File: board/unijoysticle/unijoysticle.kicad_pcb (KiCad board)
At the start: 2 copper layers, 55.6 x 41.7 mm, 14 parts, among them IC1 7405, IC2 7405, J1 DB9_Female, J2 DB9_Female, J3 Barrel_Jack, SW1 SW_Push

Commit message: board: rev B ready ??
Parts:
- moved J3 0.85 mm to (161.2, 113.9)
- moved D3 0.38 mm to (160.5, 103.9)
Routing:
- net J2UP: track 14.1 -> 11.1 mm
- net GPIO_J2DOWN: track 12.4 -> 10.5 mm
- net GPIO_J2UP: track 13.1 -> 15.0 mm
- net J2RIGHT: track 27.4 -> 25.7 mm
- net GPIO_J1POTY: track 26.1 -> 27.6 mm
- net GPIO_J2FIRE: track 20.7 -> 22.2 mm
- net VDD: track 76.6 -> 77.9 mm
- net J1POTY: track 45.6 -> 45.1 mm

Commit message: layout: Rev C: Work in progress
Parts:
- removed G***: LOGO, Parts:unijoysticle_logo
- removed REF**: OSHW-Logo2_7.3x6mm_SilkScreen, Symbol:OSHW-Logo2_7.3x6mm_SilkScreen
- added D4: 1N4001, Diode_THT:D_DO-41_SOD81_P7.62mm_Horizontal, F.Cu at (153.7, 83.8)
- added SW2: SW_SPST, Button_Switch_THT:SW_DIP_SPSTx01_Slide_6.7x4.1mm_W7.62mm_P2.54mm_LowProfile, F.Cu at (133.3, 83.8)
- R1, R2: value 100 -> 150
- moved J3 3.24 mm to (162.6, 116.8)
- moved SW1 3.13 mm to (115.0, 116.5)
- moved R2 2.95 mm to (124.5, 118.0)
- moved R1 2.88 mm to (121.9, 118.0)
- moved B1 2.54 mm to (127.3, 125.7)
- moved D3 1.70 mm to (161.3, 105.4)
- moved IC1 1.52 mm to (115.6, 83.4)
- moved D1 1.45 mm to (116.8, 105.4)
- moved D2 1.26 mm to (123.2, 105.4)
- moved IC2 0.76 mm to (161.3, 83.4)
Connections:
- IC1 pad 14: VDD -> J1POWER
- IC2 pad 14: VDD -> Net-(IC2-Pad14)
- J1 pad 7: Net-(J1-Pad7) -> J1POWER
- J2 pad 7: Net-(J2-Pad7) -> J1POWER
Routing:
- net VDD: track 77.9 -> 0.00 mm
- net J1POTY: track 45.1 -> 0.00 mm
- net GPIO_J1POTY: track 27.6 -> 0.00 mm
- net J1FIRE: track 26.1 -> 0.00 mm
- net J2RIGHT: track 25.7 -> 0.00 mm
- net J2FIRE: track 25.5 -> 0.00 mm
- net GPIO_J1POTX: track 25.1 -> 0.00 mm
- net J1RIGHT: track 24.2 -> 0.00 mm
- net GPIO_J2FIRE: track 22.2 -> 0.00 mm
- net J1LEFT: track 21.8 -> 0.00 mm
- net GPIO_J1UP: track 20.9 -> 0.00 mm
- net J2LEFT: track 20.0 -> 0.00 mm
- net GPIO_J1FIRE: track 19.7 -> 0.00 mm
- net GPIO_J1DOWN: track 18.9 -> 0.00 mm
- net J1DOWN: track 17.5 -> 0.00 mm
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- removed copper zone on B.Cu, net GND
- removed copper zone on F.Cu, net GND
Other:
- board size 55.6 x 41.7 mm -> 58 x 44.4 mm
- board text added: "Rev C"
- board text removed: "Rev B"

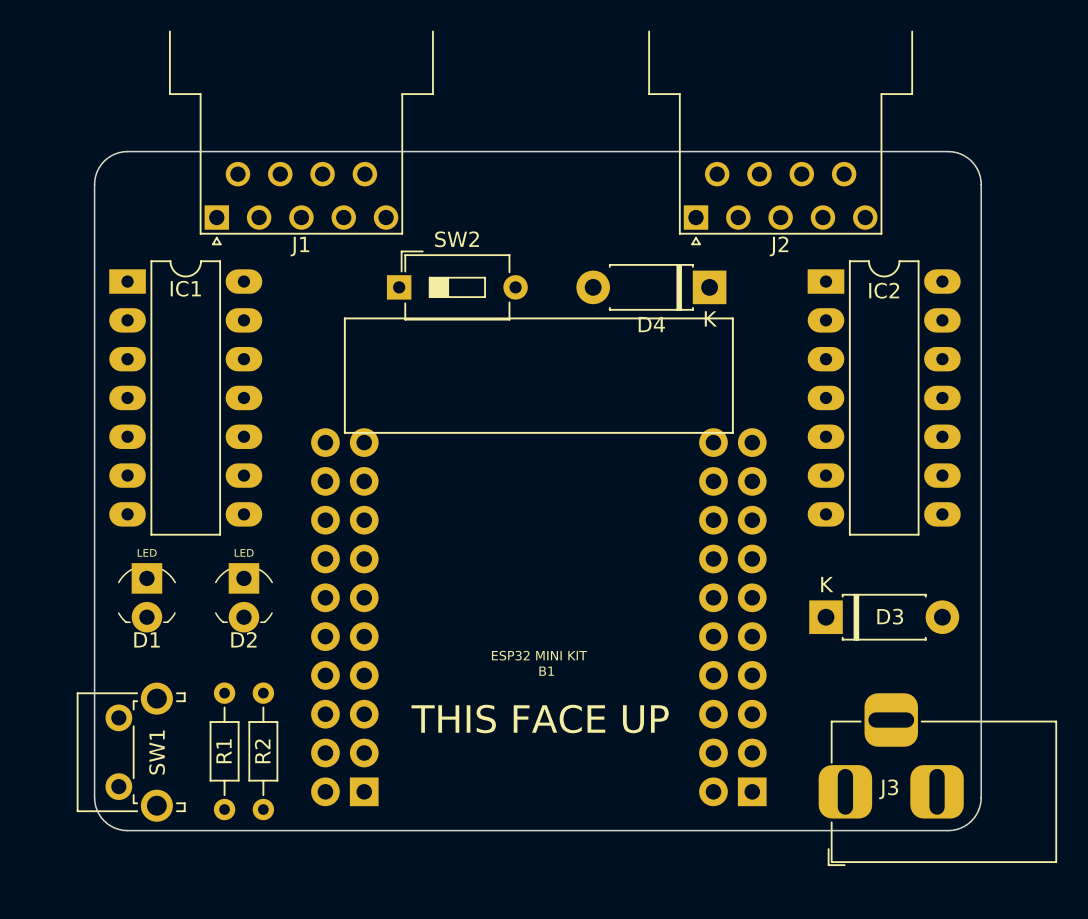
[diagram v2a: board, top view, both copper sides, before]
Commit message: layout / schematic: replaced 7405 model with one with comes with pwr/gnd
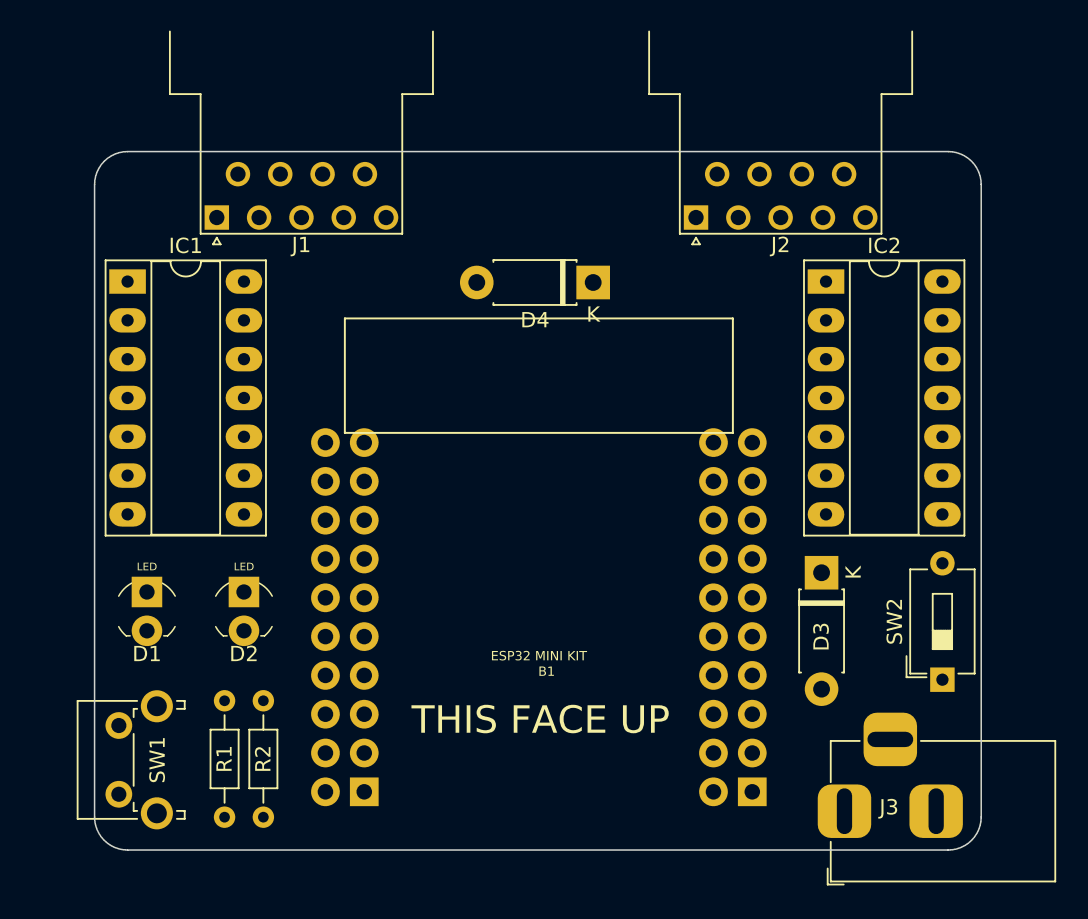
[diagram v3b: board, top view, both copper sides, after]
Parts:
- IC1, IC2: value 7405 -> 74LS05; footprint Package_DIP:DIP-14_W7.62mm_LongPads -> Package_DIP:DIP-14_W7.62mm_Socket_LongPads
- moved SW2 43.9 mm to (168.9, 109.5), turned to 90 degrees
- moved D4 7.63 mm to (146.1, 83.5)
- moved D3 2.92 mm to (161.0, 102.5), turned to 270 degrees
- moved J3 1.27 mm to (162.5, 118.1)
- moved D1 0.89 mm to (116.8, 106.3)
- moved D2 0.89 mm to (123.2, 106.3)
- moved R1 0.50 mm to (121.9, 118.5)
- moved R2 0.50 mm to (124.5, 118.5)
- moved SW1 0.50 mm to (115.0, 117.0)
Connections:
- B1 pad 11: Net-(B1-Pad11) -> (no net)
- B1 pad 15: Net-(B1-Pad15) -> (no net)
- B1 pad 21: Net-(B1-Pad21) -> (no net)
- B1 pad 22: Net-(B1-Pad22) -> (no net)
- B1 pad 3: Net-(B1-Pad3) -> (no net)
- B1 pad 34: Net-(B1-Pad34) -> (no net)
- B1 pad 35: Net-(B1-Pad35) -> (no net)
- B1 pad 36: Net-(B1-Pad36) -> (no net)
- B1 pad 39: Net-(B1-Pad39) -> (no net)
- B1 pad 4: Net-(B1-Pad4) -> (no net)
- B1 pad 6: Net-(B1-Pad6) -> (no net)
- B1 pad 7: Net-(B1-Pad7) -> (no net)
- B1 pad 8: Net-(B1-Pad8) -> (no net)
- B1 pad 9: Net-(B1-Pad9) -> (no net)
- D4 pad 1: VDD -> Net-(D4-Pad1)
- D4 pad 2: Net-(D4-Pad2) -> J1POWER
- IC2 pad 14: Net-(IC2-Pad14) -> J1POWER
- J2 pad 5: Net-(J2-Pad5) -> (no net)
- J2 pad 9: Net-(J2-Pad9) -> (no net)
- SW2 pad 1: J1POWER -> VDD
- SW2 pad 2: Net-(D4-Pad2) -> Net-(D4-Pad1)
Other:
- board size 58 x 44.4 mm -> 58 x 45.7 mm

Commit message: board: import unijoysticle logo
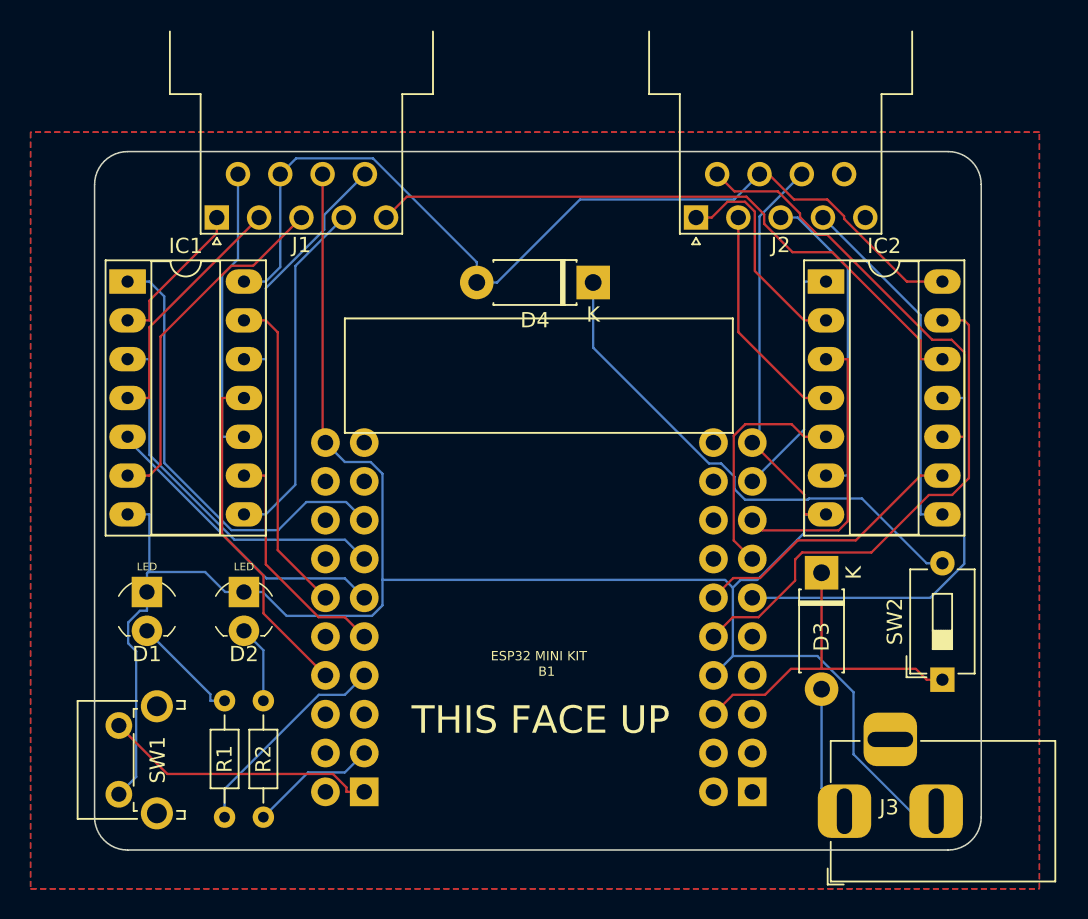
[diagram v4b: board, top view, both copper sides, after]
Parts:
- added G***: LOGO, Unijoysticle:unijoysticle_logo, B.Cu at (142.2, 96.5)
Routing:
- net GND: track 0.00 -> 153.5 mm
- net J1POWER: track 0.00 -> 62.7 mm
- net J1POTY: track 0.00 -> 42.5 mm
- net GPIO_J1POTY: track 0.00 -> 33.7 mm
- net Net-(D4-Pad1): track 0.00 -> 33.5 mm
- net GPIO_J1UP: track 0.00 -> 29.9 mm
- net J2FIRE: track 0.00 -> 28.1 mm
- net GPIO_J2FIRE: track 0.00 -> 27.1 mm
- net GPIO_J1DOWN: track 0.00 -> 24.6 mm
- net J2RIGHT: track 0.00 -> 23.5 mm
- net J1LEFT: track 0.00 -> 23.3 mm
- net J1RIGHT: track 0.00 -> 23.0 mm
- net VDD: track 0.00 -> 22.8 mm
- net GPIO_J1FIRE: track 0.00 -> 22.4 mm
- net GPIO_J1POTX: track 0.00 -> 21.2 mm
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- added copper zone on B.Cu, net GND
- added copper zone on F.Cu, net GND

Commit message: board: rev D
changes DIP switch for slide switch since it supports more amperage
board a tiny bit wider
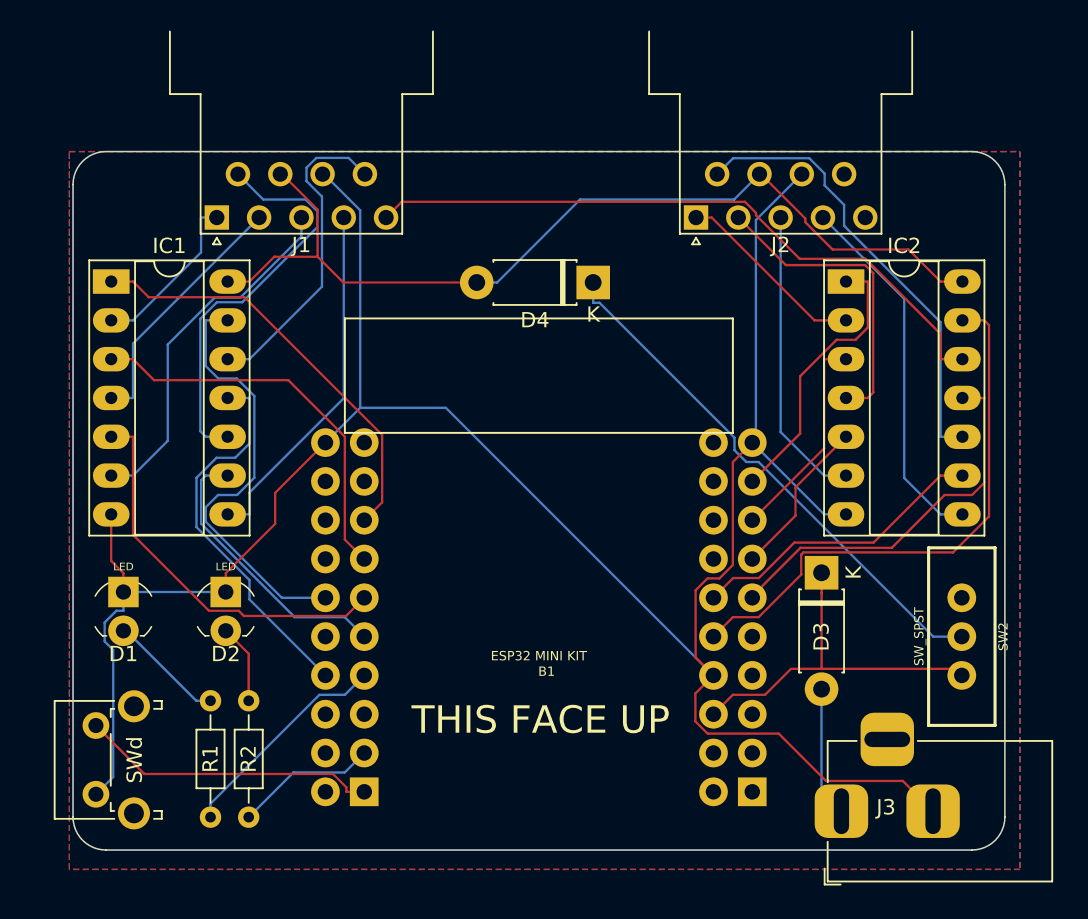
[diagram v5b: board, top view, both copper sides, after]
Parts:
- SW2: footprint Button_Switch_THT:SW_DIP_SPSTx01_Slide_6.7x4.1mm_W7.62mm_P2.54mm_LowProfile -> Switches:SWITCH_SPDT_PTH_11.6X4.0MM
- moved G*** 4.02 mm to (141.0, 92.7)
- moved SW2 3.09 mm to (170.2, 106.7), turned to 180 degrees
- moved D1 1.54 mm to (115.3, 106.3)
- moved SWd 1.50 mm to (113.5, 117.0)
- moved IC2 1.31 mm to (162.6, 83.4)
- moved D2 1.19 mm to (122.0, 106.3)
- moved IC1 1.07 mm to (114.5, 83.4)
- moved R2 0.96 mm to (123.5, 118.5)
- moved R1 0.92 mm to (121.0, 118.5)
- moved J3 0.20 mm to (162.3, 118.1)
- renumbered SW1 to SWd
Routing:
- net J1FIRE: track 19.0 -> 26.7 mm
- net GPIO_J1POTX: track 21.2 -> 28.6 mm
- net GPIO_J1LEFT: track 20.0 -> 25.7 mm
- net J2DOWN: track 15.0 -> 20.1 mm
- net GPIO_J2DOWN: track 18.8 -> 13.9 mm
- net GPIO_J2LEFT: track 15.3 -> 10.5 mm
- net J1POTX: track 16.2 -> 20.9 mm
- net GPIO_J1FIRE: track 22.4 -> 25.2 mm
- net GPIO_J1RIGHT: track 15.6 -> 18.4 mm
- net GPIO_J1POTY: track 33.7 -> 36.5 mm
- net GPIO_J2UP: track 15.9 -> 18.4 mm
- net GND: track 153.5 -> 155.5 mm
- net GPIO_J1UP: track 29.9 -> 28.0 mm
- net J2UP: track 14.4 -> 12.6 mm
- net GPIO_J2FIRE: track 27.1 -> 25.4 mm
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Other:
- board size 58 x 45.7 mm -> 61 x 45.7 mm
- board text added: "Rev D"
- board text removed: "Rev C"

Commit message: board: rev. D
replaces the DIP switch with a slide switch, right angled.
Allows better amperage, and easier to solder.
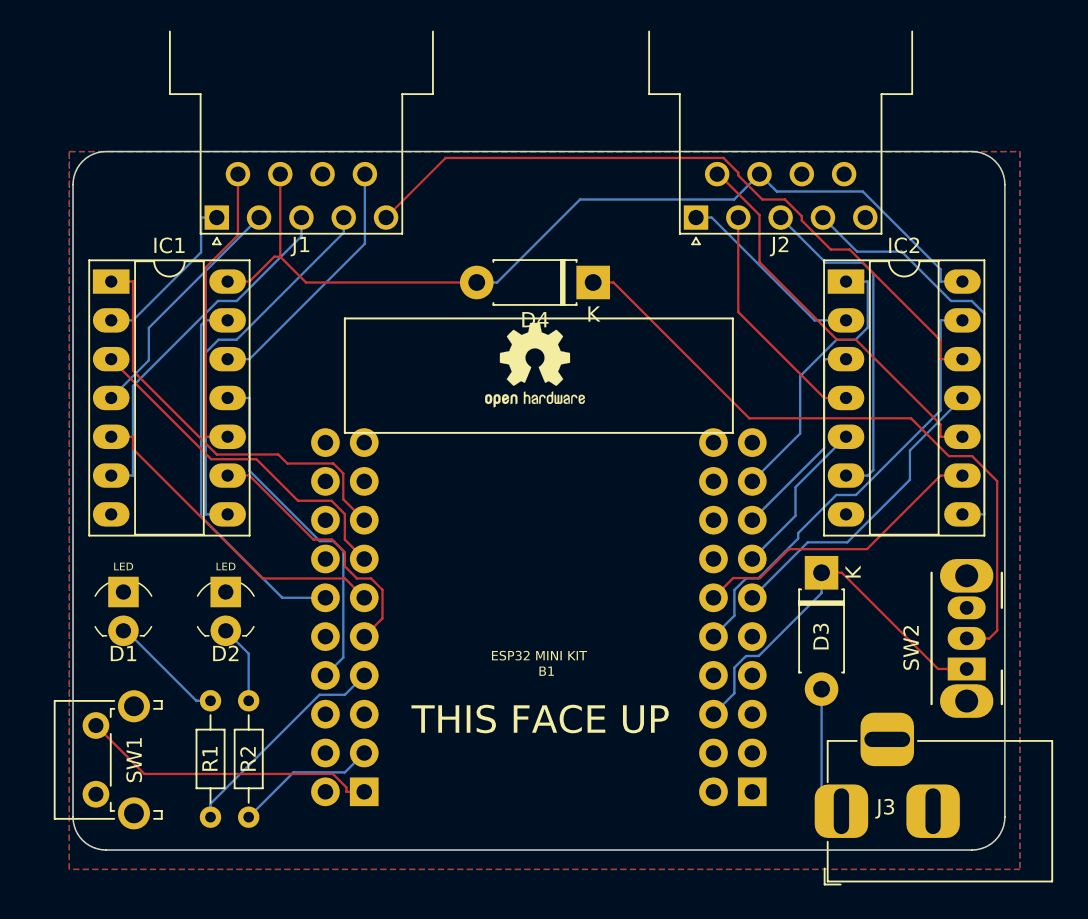
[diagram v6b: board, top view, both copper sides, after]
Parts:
- added REF**: OSHW-Logo2_7.3x6mm_SilkScreen, Symbol:OSHW-Logo2_7.3x6mm_SilkScreen, F.Cu at (142.2, 88.9)
- SW2: footprint Switches:SWITCH_SPDT_PTH_11.6X4.0MM -> Button_Switch_THT:SW_CuK_OS102011MA1QN1_SPDT_Angled
- moved SW2 2.14 mm to (170.5, 108.8), turned to 90 degrees
- moved G*** 1.80 mm to (142.2, 94.0)
- renumbered SWd to SW1
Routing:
- net GND: track 155.5 -> 0.00 mm
- net Net-(D4-Pad1): track 35.0 -> 43.8 mm
- net J1FIRE: track 26.7 -> 19.5 mm
- net GPIO_J1POTY: track 36.5 -> 29.5 mm
- net GPIO_J2FIRE: track 25.4 -> 20.3 mm
- net J2DOWN: track 20.1 -> 15.6 mm
- net GPIO_J1LEFT: track 25.7 -> 21.4 mm
- net J2FIRE: track 29.7 -> 25.5 mm
- net J1POTX: track 20.9 -> 16.7 mm
- net GPIO_J1POTX: track 28.6 -> 24.7 mm
- net J2RIGHT: track 24.0 -> 27.7 mm
- net GPIO_J1DOWN: track 25.9 -> 23.0 mm
- net J2LEFT: track 19.5 -> 22.4 mm
- net J1POTY: track 43.5 -> 45.8 mm
- net GPIO_J1FIRE: track 25.2 -> 23.1 mm
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
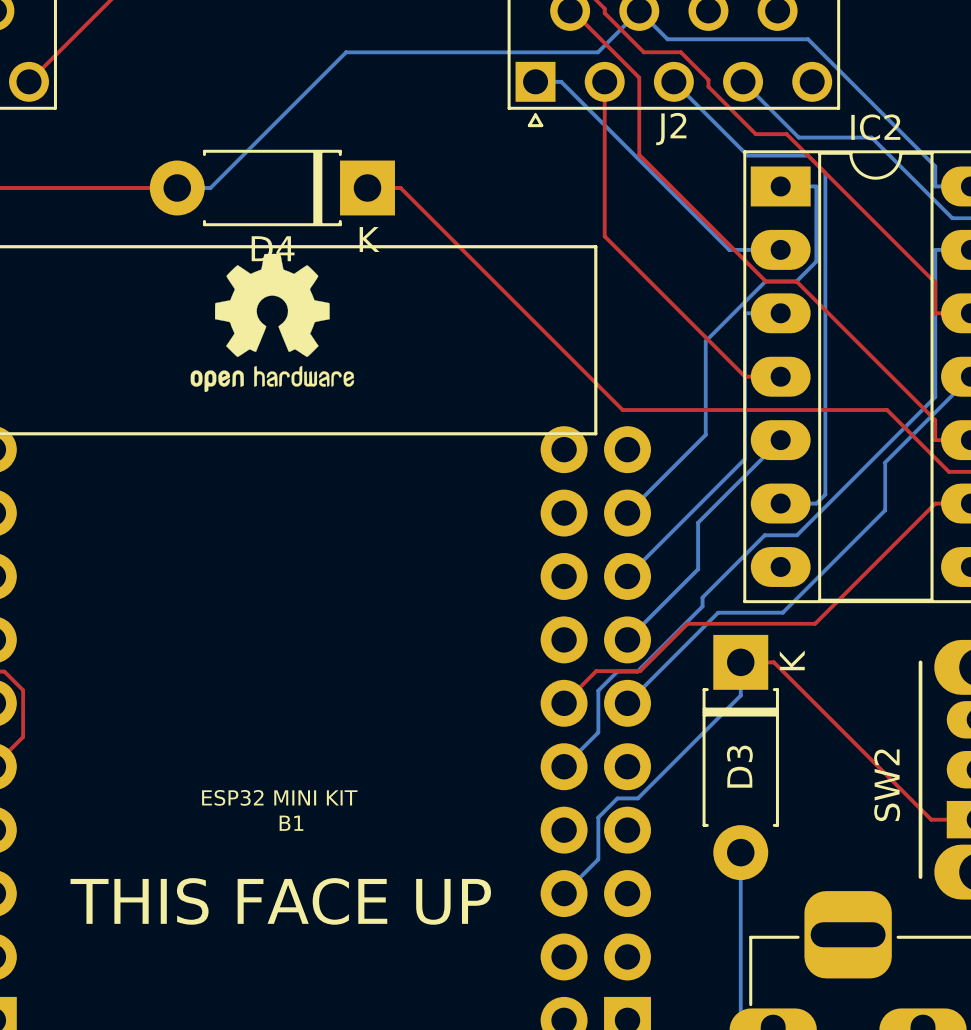
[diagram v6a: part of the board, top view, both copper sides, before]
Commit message: board: Rev F
* Use Schottky diodes
* Add mounting hole
* Logo is "locked"
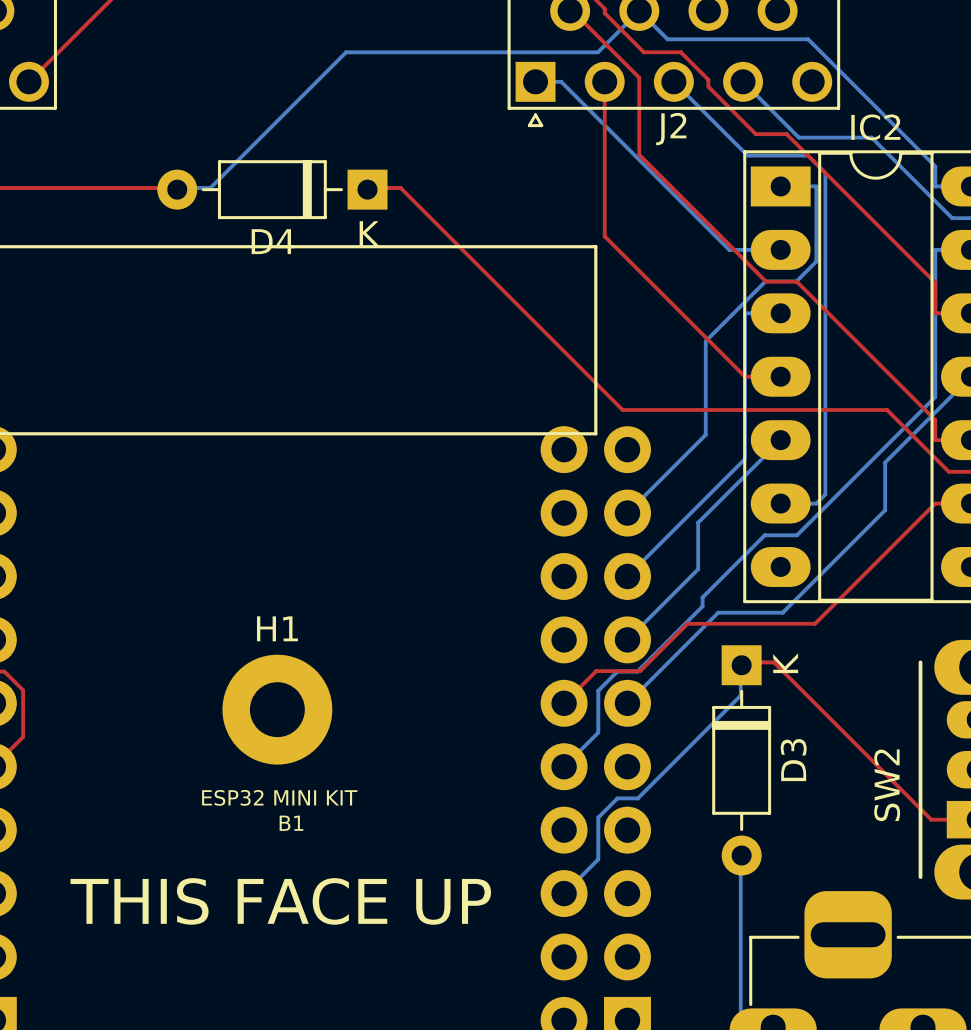
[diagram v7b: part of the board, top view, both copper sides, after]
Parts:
- removed REF**: OSHW-Logo2_7.3x6mm_SilkScreen, Symbol:OSHW-Logo2_7.3x6mm_SilkScreen
- added H1: MountingHole_Pad, MountingHole:MountingHole_2.2mm_M2_Pad, F.Cu at (142.4, 104.4)
- D3, D4: value 1N4001 -> D_Schottky; footprint Diode_THT:D_DO-41_SOD81_P7.62mm_Horizontal -> Diode_THT:D_DO-35_SOD27_P7.62mm_Horizontal
- moved D3 0.12 mm to (161.0, 102.6)
- moved D4 0.07 mm to (146.1, 83.6)
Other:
- board text added: "Rev F"
- board text removed: "Rev D"
